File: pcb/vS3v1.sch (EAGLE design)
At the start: 102 parts, among them IC1 DS3231/SO, J1 BM04B-SRSS-TB(LF)(SN), J10 48099-4000, J11 SIM8060-6-0-14-00-A, J12 S8411-45R, J13 MEM2067-02-180-00-A_REVB, J2 BM04B-SRSS-TB(LF)(SN), J3 BM04B-SRSS-TB(LF)(SN), J4 BM04B-SRSS-TB(LF)(SN), J5 BM04B-SRSS-TB(LF)(SN)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

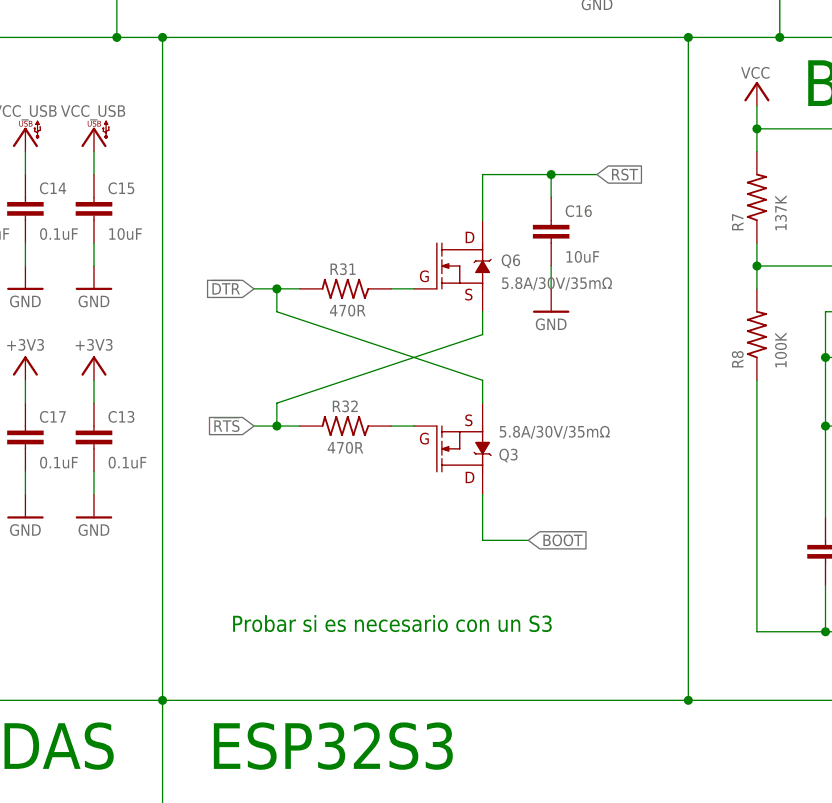
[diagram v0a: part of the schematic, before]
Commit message: feat: Add initial PCB design, schematic, and datasheet for miniMadre.
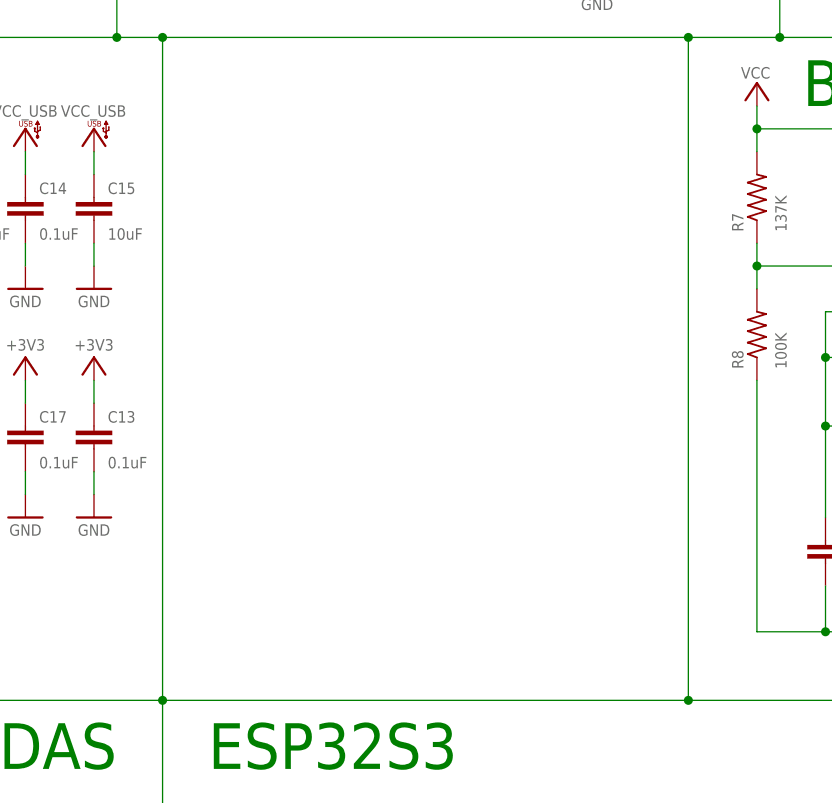
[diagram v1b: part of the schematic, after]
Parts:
- removed C16: 10uF, rcl:C-EUC0805
- removed Q3, Q6: 5.8A/30V/35mΩ, transistor:MOSFET-NCH-AO3404A
- removed R31, R32: 470R, rcl:R-US_R0805
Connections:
- removed net !DTR: Q3.S, R31.2
- removed net !RTS: Q6.S, R32.2
- removed net N$25: Q6.G, R31.1
- removed net N$26: Q3.G, R32.1
- net BOOT: no longer Q3.D
- net GND: no longer C16.2
- net RST: no longer C16.1, Q6.D
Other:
- note removed: "Probar si es necesario con un S3"
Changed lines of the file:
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@@
 <part name="P+14" library="supply" library_urn="urn:adsk.eagle:library:48476001" deviceset="VCC_USB" device=""/>
 <part name="GND20" library="superusuario_supply_multiple" deviceset="GND" device=""/>
-<part name="R31" library="rcl" library_urn="urn:adsk.eagle:library:334" deviceset="R-US_" device="R0805" package3d_urn="urn:adsk.eagle:package:23553/2" value="470R"/>
-<part name="R32" library="rcl" library_urn="urn:adsk.eagle:library:334" deviceset="R-US_" device="R0805" package3d_urn="urn:adsk.eagle:package:23553/2" value="470R"/>
-<part name="Q6" library="transistor" library_urn="urn:adsk.eagle:library:44124427" deviceset="MOSFET-NCH" device="-AO3404A" package3d_urn="urn:adsk.eagle:package:44124451/2" value="5.8A/30V/35mΩ"/>
-<part name="C16" library="rcl" library_urn="urn:adsk.eagle:library:334" deviceset="C-EU" device="C0805" package3d_urn="urn:adsk.eagle:package:23617/2" value="10uF"/>
-<part name="GND45" library="superusuario_supply_multiple" deviceset="GND" device=""/>
-<part name="Q3" library="transistor" library_urn="urn:adsk.eagle:library:44124427" deviceset="MOSFET-NCH" device="-AO3404A" package3d_urn="urn:adsk.eagle:package:44124451/2" value="5.8A/30V/35mΩ"/>
 <part name="J6" library="con-jst_sh" library_urn="urn:adsk.eagle:library:43378961" deviceset="BM02B-SRSS-TB(LF)(SN)" device="" package3d_urn="urn:adsk.eagle:package:47408583/2"/>
 <part name="C17" library="rcl" library_urn="urn:adsk.eagle:library:334" deviceset="C-EU" device="C0805" package3d_urn="urn:adsk.eagle:package:23617/2" value="0.1uF"/>
@@
 <text x="306.578" y="-4.318" size="2.54" layer="91" rot="R90">PLANTOWER</text>
 <text x="535.94" y="167.64" size="5.08" layer="91">SD</text>
-<text x="350.52" y="109.22" size="1.778" layer="91">Probar si es necesario con un S3</text>
 <text x="266.7" y="144.78" size="1.778" layer="91">No usar un ftdi usar usb directo,
 revisar si es necesario cambiar
@@
 <instance part="GND20" gate="1" x="335.28" y="147.32" smashed="yes" rot="MR0">
 <attribute name="VALUE" x="335.28" y="146.558" size="1.27" layer="96" font="vector" rot="MR0" align="top-center"/>
-</instance>
-<instance part="R31" gate="G$1" x="363.22" y="147.32" smashed="yes" rot="R180">
-<attribute name="NAME" x="364.49" y="150.1394" size="1.27" layer="95" rot="R180"/>
-<attribute name="VALUE" x="365.506" y="145.542" size="1.27" layer="96" rot="R180"/>
-</instance>
-<instance part="R32" gate="G$1" x="363.22" y="132.08" smashed="yes" rot="R180">
-<attribute name="NAME" x="364.744" y="134.8994" size="1.27" layer="95" rot="R180"/>
-<attribute name="VALUE" x="365.252" y="130.302" size="1.27" layer="96" rot="R180"/>
-</instance>
-<instance part="Q6" gate="NMOS" x="375.92" y="149.86" smashed="yes">
-<attribute name="NAME" x="380.492" y="149.86" size="1.27" layer="95" font="vector"/>
-<attribute name="VALUE" x="380.492" y="147.32" size="1.27" layer="96" font="vector"/>
-</instance>
-<instance part="C16" gate="G$1" x="386.08" y="154.94" smashed="yes">
-<attribute name="NAME" x="387.604" y="155.321" size="1.27" layer="95"/>
-<attribute name="VALUE" x="387.604" y="150.241" size="1.27" layer="96"/>
-</instance>
-<instance part="GND45" gate="1" x="386.08" y="144.78" smashed="yes">
-<attribute name="VALUE" x="386.08" y="144.018" size="1.27" layer="96" font="vector" align="top-center"/>
-</instance>
-<instance part="Q3" gate="NMOS" x="375.92" y="129.54" smashed="yes" rot="MR180">
-<attribute name="NAME" x="380.238" y="129.54" size="1.27" layer="95" font="vector" rot="MR180"/>
-<attribute name="VALUE" x="380.238" y="132.08" size="1.27" layer="96" font="vector" rot="MR180"/>
 </instance>
 <instance part="J6" gate="G$1" x="312.42" y="30.48" smashed="yes" rot="MR0">
@@
 </segment>
 <segment>
-<pinref part="C16" gate="G$1" pin="2"/>
-<wire x1="386.08" y1="149.86" x2="386.08" y2="147.32" width="0.1524" layer="91"/>
-<pinref part="GND45" gate="1" pin="GND"/>
-</segment>
-<segment>
 <pinref part="C17" gate="G$1" pin="2"/>
 <wire x1="327.66" y1="127" x2="327.66" y2="124.46" width="0.1524" layer="91"/>
@@
 </segment>
 <segment>
-<wire x1="378.46" y1="124.46" x2="378.46" y2="119.38" width="0.1524" layer="91"/>
-<wire x1="378.46" y1="119.38" x2="383.54" y2="119.38" width="0.1524" layer="91"/>
-<label x="383.54" y="119.38" size="1.27" layer="95" xref="yes"/>
-<pinref part="Q3" gate="NMOS" pin="D"/>
-</segment>
-<segment>
 <pinref part="U$4" gate="G$1" pin="IO0"/>
 <wire x1="421.64" y1="-86.36" x2="439.42" y2="-86.36" width="0.1524" layer="91"/>
@@
 <junction x="355.6" y="68.58"/>
 <label x="353.06" y="68.58" size="1.27" layer="95" rot="R180" xref="yes"/>
-</segment>
-<segment>
-<wire x1="378.46" y1="154.94" x2="378.46" y2="160.02" width="0.1524" layer="91"/>
-<wire x1="378.46" y1="160.02" x2="386.08" y2="160.02" width="0.1524" layer="91"/>
-<label x="391.16" y="160.02" size="1.27" layer="95" xref="yes"/>
-<pinref part="Q6" gate="NMOS" pin="D"/>
-<pinref part="C16" gate="G$1" pin="1"/>
-<wire x1="386.08" y1="160.02" x2="391.16" y2="160.02" width="0.1524" layer="91"/>
-<wire x1="386.08" y1="157.48" x2="386.08" y2="160.02" width="0.1524" layer="91"/>
-<junction x="386.08" y="160.02"/>
 </segment>
 <segment>
@@
 </segment>
 </net>
-<net name="!DTR" class="0">
-<segment>
-<wire x1="378.46" y1="134.62" x2="378.46" y2="137.16" width="0.1524" layer="91"/>
-<pinref part="R31" gate="G$1" pin="2"/>
-<wire x1="358.14" y1="147.32" x2="355.6" y2="147.32" width="0.1524" layer="91"/>
-<wire x1="355.6" y1="147.32" x2="355.6" y2="144.78" width="0.1524" layer="91"/>
-<junction x="355.6" y="147.32"/>
-<wire x1="378.46" y1="137.16" x2="355.6" y2="144.78" width="0.1524" layer="91"/>
-<wire x1="355.6" y1="147.32" x2="353.06" y2="147.32" width="0.1524" layer="91"/>
-<pinref part="Q3" gate="NMOS" pin="S"/>
-<label x="353.06" y="147.32" size="1.27" layer="95" rot="R180" xref="yes"/>
-</segment>
-</net>
-<net name="!RTS" class="0">
-<segment>
-<pinref part="R32" gate="G$1" pin="2"/>
-<wire x1="358.14" y1="132.08" x2="355.6" y2="132.08" width="0.1524" layer="91"/>
-<wire x1="355.6" y1="132.08" x2="355.6" y2="134.62" width="0.1524" layer="91"/>
-<junction x="355.6" y="132.08"/>
-<wire x1="378.46" y1="144.78" x2="378.46" y2="142.24" width="0.1524" layer="91"/>
-<wire x1="355.6" y1="134.62" x2="378.46" y2="142.24" width="0.1524" layer="91"/>
-<wire x1="355.6" y1="132.08" x2="353.06" y2="132.08" width="0.1524" layer="91"/>
-<pinref part="Q6" gate="NMOS" pin="S"/>
-<label x="353.06" y="132.08" size="1.27" layer="95" rot="R180" xref="yes"/>
-</segment>
-</net>
-<net name="N$25" class="0">
-<segment>
-<wire x1="370.84" y1="147.32" x2="368.3" y2="147.32" width="0.1524" layer="91"/>
-<pinref part="R31" gate="G$1" pin="1"/>
-<pinref part="Q6" gate="NMOS" pin="G"/>
-</segment>
-</net>
-<net name="N$26" class="0">
-<segment>
-<wire x1="368.3" y1="132.08" x2="370.84" y2="132.08" width="0.1524" layer="91"/>
-<pinref part="R32" gate="G$1" pin="1"/>
-<pinref part="Q3" gate="NMOS" pin="G"/>
-</segment>
-</net>

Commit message: Save local changes (PCB update, PDF remove)
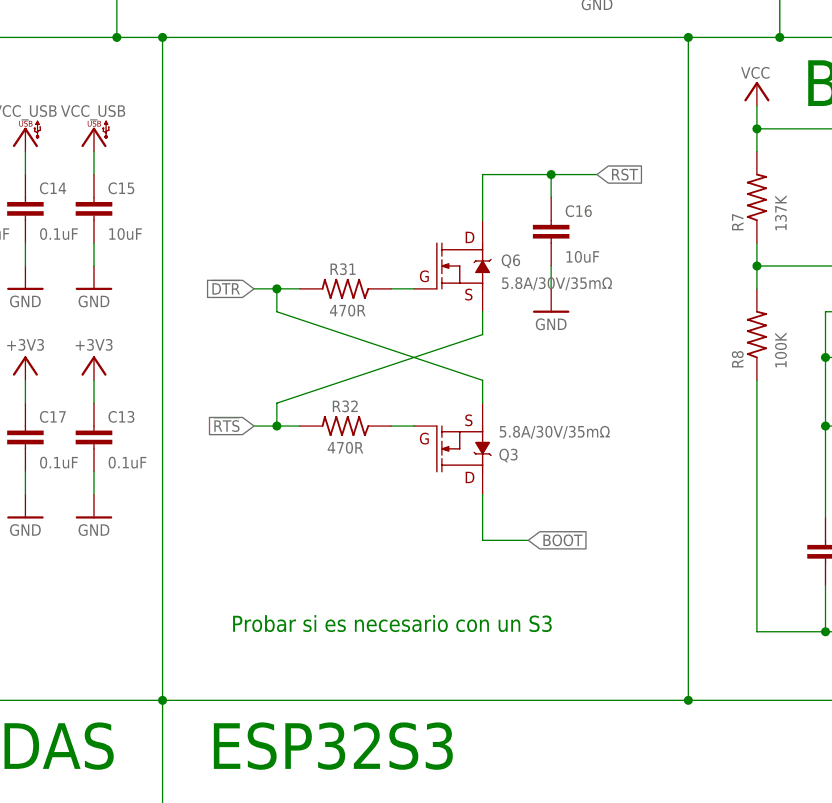
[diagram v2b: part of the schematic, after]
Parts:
- added C16: 10uF, rcl:C-EUC0805
- added Q3, Q6: 5.8A/30V/35mΩ, transistor:MOSFET-NCH-AO3404A
- added R31, R32: 470R, rcl:R-US_R0805
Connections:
- new net !DTR: Q3.S, R31.2
- new net !RTS: Q6.S, R32.2
- new net N$25: Q6.G, R31.1
- new net N$26: Q3.G, R32.1
- net BOOT: now also Q3.D
- net GND: now also C16.2
- net RST: now also C16.1, Q6.D
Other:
- note added: "Probar si es necesario con un S3"
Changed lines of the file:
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@@
 <part name="P+14" library="supply" library_urn="urn:adsk.eagle:library:48476001" deviceset="VCC_USB" device=""/>
 <part name="GND20" library="superusuario_supply_multiple" deviceset="GND" device=""/>
+<part name="R31" library="rcl" library_urn="urn:adsk.eagle:library:334" deviceset="R-US_" device="R0805" package3d_urn="urn:adsk.eagle:package:23553/2" value="470R"/>
+<part name="R32" library="rcl" library_urn="urn:adsk.eagle:library:334" deviceset="R-US_" device="R0805" package3d_urn="urn:adsk.eagle:package:23553/2" value="470R"/>
+<part name="Q6" library="transistor" library_urn="urn:adsk.eagle:library:44124427" deviceset="MOSFET-NCH" device="-AO3404A" package3d_urn="urn:adsk.eagle:package:44124451/2" value="5.8A/30V/35mΩ"/>
+<part name="C16" library="rcl" library_urn="urn:adsk.eagle:library:334" deviceset="C-EU" device="C0805" package3d_urn="urn:adsk.eagle:package:23617/2" value="10uF"/>
+<part name="GND45" library="superusuario_supply_multiple" deviceset="GND" device=""/>
+<part name="Q3" library="transistor" library_urn="urn:adsk.eagle:library:44124427" deviceset="MOSFET-NCH" device="-AO3404A" package3d_urn="urn:adsk.eagle:package:44124451/2" value="5.8A/30V/35mΩ"/>
 <part name="J6" library="con-jst_sh" library_urn="urn:adsk.eagle:library:43378961" deviceset="BM02B-SRSS-TB(LF)(SN)" device="" package3d_urn="urn:adsk.eagle:package:47408583/2"/>
 <part name="C17" library="rcl" library_urn="urn:adsk.eagle:library:334" deviceset="C-EU" device="C0805" package3d_urn="urn:adsk.eagle:package:23617/2" value="0.1uF"/>
@@
 <text x="306.578" y="-4.318" size="2.54" layer="91" rot="R90">PLANTOWER</text>
 <text x="535.94" y="167.64" size="5.08" layer="91">SD</text>
+<text x="350.52" y="109.22" size="1.778" layer="91">Probar si es necesario con un S3</text>
 <text x="266.7" y="144.78" size="1.778" layer="91">No usar un ftdi usar usb directo,
 revisar si es necesario cambiar
@@
 <instance part="GND20" gate="1" x="335.28" y="147.32" smashed="yes" rot="MR0">
 <attribute name="VALUE" x="335.28" y="146.558" size="1.27" layer="96" font="vector" rot="MR0" align="top-center"/>
+</instance>
+<instance part="R31" gate="G$1" x="363.22" y="147.32" smashed="yes" rot="R180">
+<attribute name="NAME" x="364.49" y="150.1394" size="1.27" layer="95" rot="R180"/>
+<attribute name="VALUE" x="365.506" y="145.542" size="1.27" layer="96" rot="R180"/>
+</instance>
+<instance part="R32" gate="G$1" x="363.22" y="132.08" smashed="yes" rot="R180">
+<attribute name="NAME" x="364.744" y="134.8994" size="1.27" layer="95" rot="R180"/>
+<attribute name="VALUE" x="365.252" y="130.302" size="1.27" layer="96" rot="R180"/>
+</instance>
+<instance part="Q6" gate="NMOS" x="375.92" y="149.86" smashed="yes">
+<attribute name="NAME" x="380.492" y="149.86" size="1.27" layer="95" font="vector"/>
+<attribute name="VALUE" x="380.492" y="147.32" size="1.27" layer="96" font="vector"/>
+</instance>
+<instance part="C16" gate="G$1" x="386.08" y="154.94" smashed="yes">
+<attribute name="NAME" x="387.604" y="155.321" size="1.27" layer="95"/>
+<attribute name="VALUE" x="387.604" y="150.241" size="1.27" layer="96"/>
+</instance>
+<instance part="GND45" gate="1" x="386.08" y="144.78" smashed="yes">
+<attribute name="VALUE" x="386.08" y="144.018" size="1.27" layer="96" font="vector" align="top-center"/>
+</instance>
+<instance part="Q3" gate="NMOS" x="375.92" y="129.54" smashed="yes" rot="MR180">
+<attribute name="NAME" x="380.238" y="129.54" size="1.27" layer="95" font="vector" rot="MR180"/>
+<attribute name="VALUE" x="380.238" y="132.08" size="1.27" layer="96" font="vector" rot="MR180"/>
 </instance>
 <instance part="J6" gate="G$1" x="312.42" y="30.48" smashed="yes" rot="MR0">
@@
 </segment>
 <segment>
+<pinref part="C16" gate="G$1" pin="2"/>
+<wire x1="386.08" y1="149.86" x2="386.08" y2="147.32" width="0.1524" layer="91"/>
+<pinref part="GND45" gate="1" pin="GND"/>
+</segment>
+<segment>
 <pinref part="C17" gate="G$1" pin="2"/>
 <wire x1="327.66" y1="127" x2="327.66" y2="124.46" width="0.1524" layer="91"/>
@@
 </segment>
 <segment>
+<wire x1="378.46" y1="124.46" x2="378.46" y2="119.38" width="0.1524" layer="91"/>
+<wire x1="378.46" y1="119.38" x2="383.54" y2="119.38" width="0.1524" layer="91"/>
+<label x="383.54" y="119.38" size="1.27" layer="95" xref="yes"/>
+<pinref part="Q3" gate="NMOS" pin="D"/>
+</segment>
+<segment>
 <pinref part="U$4" gate="G$1" pin="IO0"/>
 <wire x1="421.64" y1="-86.36" x2="439.42" y2="-86.36" width="0.1524" layer="91"/>
@@
 <junction x="355.6" y="68.58"/>
 <label x="353.06" y="68.58" size="1.27" layer="95" rot="R180" xref="yes"/>
+</segment>
+<segment>
+<wire x1="378.46" y1="154.94" x2="378.46" y2="160.02" width="0.1524" layer="91"/>
+<wire x1="378.46" y1="160.02" x2="386.08" y2="160.02" width="0.1524" layer="91"/>
+<label x="391.16" y="160.02" size="1.27" layer="95" xref="yes"/>
+<pinref part="Q6" gate="NMOS" pin="D"/>
+<pinref part="C16" gate="G$1" pin="1"/>
+<wire x1="386.08" y1="160.02" x2="391.16" y2="160.02" width="0.1524" layer="91"/>
+<wire x1="386.08" y1="157.48" x2="386.08" y2="160.02" width="0.1524" layer="91"/>
+<junction x="386.08" y="160.02"/>
 </segment>
 <segment>
@@
 </segment>
 </net>
+<net name="!DTR" class="0">
+<segment>
+<wire x1="378.46" y1="134.62" x2="378.46" y2="137.16" width="0.1524" layer="91"/>
+<pinref part="R31" gate="G$1" pin="2"/>
+<wire x1="358.14" y1="147.32" x2="355.6" y2="147.32" width="0.1524" layer="91"/>
+<wire x1="355.6" y1="147.32" x2="355.6" y2="144.78" width="0.1524" layer="91"/>
+<junction x="355.6" y="147.32"/>
+<wire x1="378.46" y1="137.16" x2="355.6" y2="144.78" width="0.1524" layer="91"/>
+<wire x1="355.6" y1="147.32" x2="353.06" y2="147.32" width="0.1524" layer="91"/>
+<pinref part="Q3" gate="NMOS" pin="S"/>
+<label x="353.06" y="147.32" size="1.27" layer="95" rot="R180" xref="yes"/>
+</segment>
+</net>
+<net name="!RTS" class="0">
+<segment>
+<pinref part="R32" gate="G$1" pin="2"/>
+<wire x1="358.14" y1="132.08" x2="355.6" y2="132.08" width="0.1524" layer="91"/>
+<wire x1="355.6" y1="132.08" x2="355.6" y2="134.62" width="0.1524" layer="91"/>
+<junction x="355.6" y="132.08"/>
+<wire x1="378.46" y1="144.78" x2="378.46" y2="142.24" width="0.1524" layer="91"/>
+<wire x1="355.6" y1="134.62" x2="378.46" y2="142.24" width="0.1524" layer="91"/>
+<wire x1="355.6" y1="132.08" x2="353.06" y2="132.08" width="0.1524" layer="91"/>
+<pinref part="Q6" gate="NMOS" pin="S"/>
+<label x="353.06" y="132.08" size="1.27" layer="95" rot="R180" xref="yes"/>
+</segment>
+</net>
+<net name="N$25" class="0">
+<segment>
+<wire x1="370.84" y1="147.32" x2="368.3" y2="147.32" width="0.1524" layer="91"/>
+<pinref part="R31" gate="G$1" pin="1"/>
+<pinref part="Q6" gate="NMOS" pin="G"/>
+</segment>
+</net>
+<net name="N$26" class="0">
+<segment>
+<wire x1="368.3" y1="132.08" x2="370.84" y2="132.08" width="0.1524" layer="91"/>
+<pinref part="R32" gate="G$1" pin="1"/>
+<pinref part="Q3" gate="NMOS" pin="G"/>
+</segment>
+</net>
